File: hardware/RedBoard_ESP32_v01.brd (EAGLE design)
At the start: 68.6 x 58.4 mm, 211 parts, among them J1 5.5x2.1mm Barrel, J13 QWIIC_RIGHT_ANGLE, J15 MICRO-SD-PUSH-PUSH-EXT-PIN, J2 USB C, J3 USB_SOLDER_PADS, J5 M10NO_SILK, Q1 MBT3904DW1T1, Q11 20V/4.2A/52mΩ/1.4W, Q13 20V/4.2A/52mΩ/1.4W, Q3 20V/4.2A/52mΩ/1.4W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

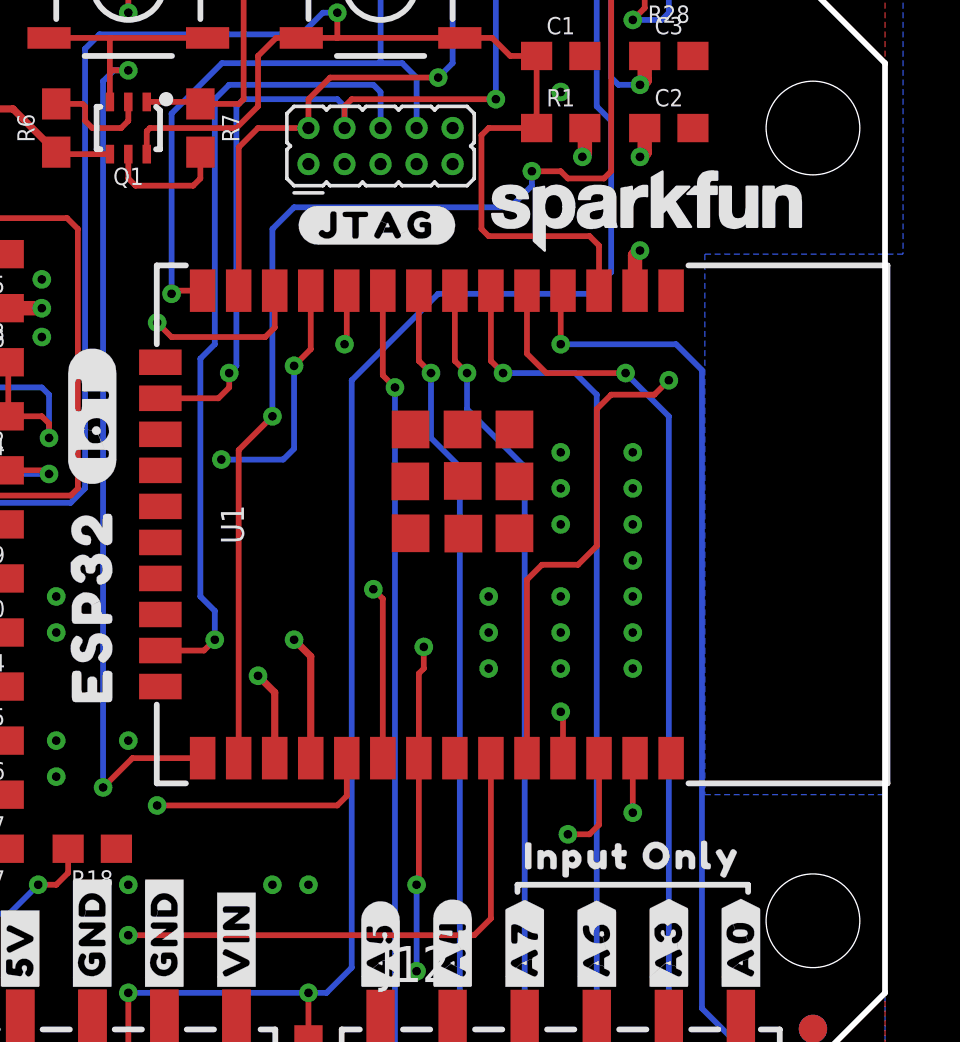
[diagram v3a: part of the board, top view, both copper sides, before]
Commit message: Updated silkscreen.
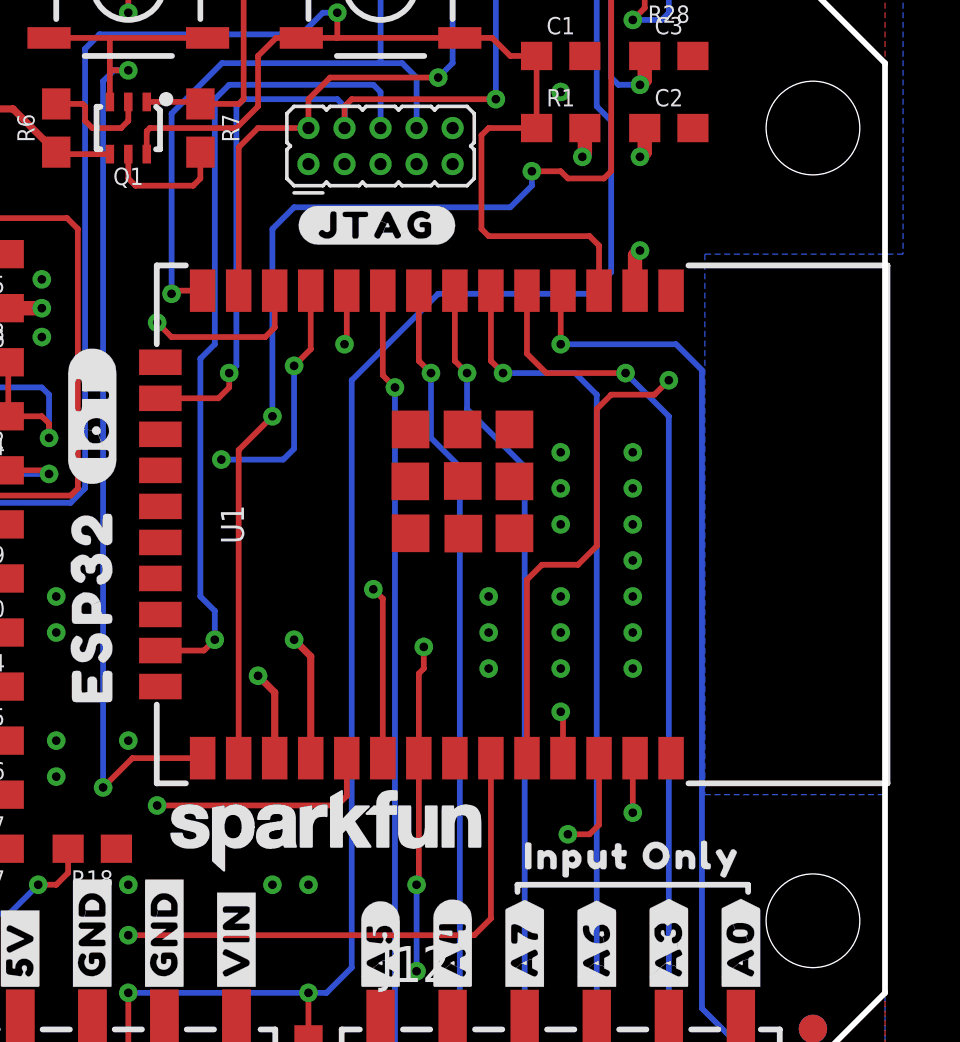
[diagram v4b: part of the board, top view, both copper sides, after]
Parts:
- moved LOGO1 24.6 mm to (48.9, 13.3)
- moved U$47 11.3 mm to (26.2, 32.6)
- moved U$93 1.91 mm to (40.0, 21.5)
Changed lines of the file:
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@@
 <drawing>
 <settings>
-<setting alwaysvectorfont="no"/>
+<setting alwaysvectorfont="yes"/>
 <setting keepoldvectorfont="yes"/>
 <setting verticaltext="up"/>
@@
 <grid distance="0.05" unitdist="inch" unit="inch" style="lines" multiple="1" display="yes" altdistance="0.005" altunitdist="inch" altunit="inch"/>
 <layers>
-<layer number="1" name="Top" color="4" fill="1" visible="yes" active="yes"/>
-<layer number="2" name="Route2" color="24" fill="1" visible="yes" active="yes"/>
-<layer number="15" name="Route15" color="23" fill="1" visible="yes" active="yes"/>
-<layer number="16" name="Bottom" color="1" fill="1" visible="yes" active="yes"/>
-<layer number="17" name="Pads" color="2" fill="1" visible="yes" active="yes"/>
-<layer number="18" name="Vias" color="2" fill="1" visible="yes" active="yes"/>
-<layer number="19" name="Unrouted" color="6" fill="1" visible="yes" active="yes"/>
+<layer number="1" name="Top" color="4" fill="1" visible="no" active="yes"/>
+<layer number="2" name="Route2" color="24" fill="1" visible="no" active="yes"/>
+<layer number="15" name="Route15" color="23" fill="1" visible="no" active="yes"/>
+<layer number="16" name="Bottom" color="1" fill="1" visible="no" active="yes"/>
+<layer number="17" name="Pads" color="2" fill="1" visible="no" active="yes"/>
+<layer number="18" name="Vias" color="2" fill="1" visible="no" active="yes"/>
+<layer number="19" name="Unrouted" color="6" fill="1" visible="no" active="yes"/>
 <layer number="20" name="Dimension" color="24" fill="1" visible="yes" active="yes"/>
 <layer number="21" name="tPlace" color="16" fill="1" visible="yes" active="yes"/>
@@
 <layer number="23" name="tOrigins" color="15" fill="1" visible="yes" active="yes"/>
 <layer number="24" name="bOrigins" color="15" fill="1" visible="yes" active="yes"/>
-<layer number="25" name="tNames" color="7" fill="1" visible="yes" active="yes"/>
-<layer number="26" name="bNames" color="7" fill="1" visible="yes" active="yes"/>
-<layer number="27" name="tValues" color="7" fill="1" visible="yes" active="yes"/>
-<layer number="28" name="bValues" color="7" fill="1" visible="yes" active="yes"/>
-<layer number="29" name="tStop" color="7" fill="3" visible="yes" active="yes"/>
-<layer number="30" name="bStop" color="7" fill="6" visible="yes" active="yes"/>
-<layer number="31" name="tCream" color="7" fill="4" visible="yes" active="yes"/>
-<layer number="32" name="bCream" color="7" fill="5" visible="yes" active="yes"/>
-<layer number="33" name="tFinish" color="6" fill="3" visible="yes" active="yes"/>
-<layer number="34" name="bFinish" color="6" fill="6" visible="yes" active="yes"/>
-<layer number="35" name="tGlue" color="7" fill="4" visible="yes" active="yes"/>
-<layer number="36" name="bGlue" color="7" fill="5" visible="yes" active="yes"/>
-<layer number="37" name="tTest" color="7" fill="1" visible="yes" active="yes"/>
-<layer number="38" name="bTest" color="7" fill="1" visible="yes" active="yes"/>
-<layer number="39" name="tKeepout" color="4" fill="11" visible="yes" active="yes"/>
-<layer number="40" name="bKeepout" color="1" fill="11" visible="yes" active="yes"/>
-<layer number="41" name="tRestrict" color="4" fill="10" visible="yes" active="yes"/>
-<layer number="42" name="bRestrict" color="1" fill="10" visible="yes" active="yes"/>
-<layer number="43" name="vRestrict" color="2" fill="10" visible="yes" active="yes"/>
-<layer number="44" name="Drills" color="7" fill="1" visible="yes" active="yes"/>
-<layer number="45" name="Holes" color="7" fill="1" visible="yes" active="yes"/>
-<layer number="46" name="Milling" color="3" fill="1" visible="yes" active="yes"/>
-<layer number="47" name="Measures" color="7" fill="1" visible="yes" active="yes"/>
+<layer number="25" name="tNames" color="7" fill="1" visible="no" active="yes"/>
+<layer number="26" name="bNames" color="7" fill="1" visible="no" active="yes"/>
+<layer number="27" name="tValues" color="7" fill="1" visible="no" active="yes"/>
+<layer number="28" name="bValues" color="7" fill="1" visible="no" active="yes"/>
+<layer number="29" name="tStop" color="7" fill="3" visible="no" active="yes"/>
+<layer number="30" name="bStop" color="7" fill="6" visible="no" active="yes"/>
+<layer number="31" name="tCream" color="7" fill="4" visible="no" active="yes"/>
+<layer number="32" name="bCream" color="7" fill="5" visible="no" active="yes"/>
+<layer number="33" name="tFinish" color="6" fill="3" visible="no" active="yes"/>
+<layer number="34" name="bFinish" color="6" fill="6" visible="no" active="yes"/>
+<layer number="35" name="tGlue" color="7" fill="4" visible="no" active="yes"/>
+<layer number="36" name="bGlue" color="7" fill="5" visible="no" active="yes"/>
+<layer number="37" name="tTest" color="7" fill="1" visible="no" active="yes"/>
+<layer number="38" name="bTest" color="7" fill="1" visible="no" active="yes"/>
+<layer number="39" name="tKeepout" color="4" fill="11" visible="no" active="yes"/>
+<layer number="40" name="bKeepout" color="1" fill="11" visible="no" active="yes"/>
+<layer number="41" name="tRestrict" color="4" fill="10" visible="no" active="yes"/>
+<layer number="42" name="bRestrict" color="1" fill="10" visible="no" active="yes"/>
+<layer number="43" name="vRestrict" color="2" fill="10" visible="no" active="yes"/>
+<layer number="44" name="Drills" color="7" fill="1" visible="no" active="yes"/>
+<layer number="45" name="Holes" color="7" fill="1" visible="no" active="yes"/>
+<layer number="46" name="Milling" color="3" fill="1" visible="no" active="yes"/>
+<layer number="47" name="Measures" color="7" fill="1" visible="no" active="yes"/>
 <layer number="48" name="Document" color="7" fill="1" visible="yes" active="yes"/>
-<layer number="49" name="Reference" color="7" fill="1" visible="yes" active="yes"/>
-<layer number="50" name="dxf" color="7" fill="1" visible="yes" active="yes"/>
+<layer number="49" name="Reference" color="7" fill="1" visible="no" active="yes"/>
+<layer number="50" name="dxf" color="7" fill="1" visible="no" active="yes"/>
 <layer number="51" name="tDocu" color="6" fill="1" visible="yes" active="yes"/>
 <layer number="52" name="bDocu" color="7" fill="1" visible="yes" active="yes"/>
@@
 <attribute name="VALUE" x="31.75" y="38.4175" size="0.6096" layer="27" font="vector" ratio="20" rot="R180" align="top-center"/>
 </element>
-<element name="LOGO1" library="SparkFun-Aesthetics" package="SFE_LOGO_NAME_.1" value="SFE_LOGO_NAME.1_INCH" x="60.198" y="35.179" smashed="yes"/>
+<element name="LOGO1" library="SparkFun-Aesthetics" package="SFE_LOGO_NAME_.1" value="SFE_LOGO_NAME.1_INCH" x="48.895" y="13.335" smashed="yes"/>
 <element name="LOGO2" library="SparkFun-Aesthetics" package="QWIIC_5MM" value="QWIIC_LOGO_5MM" x="10.16" y="51.562" smashed="yes"/>
 <element name="LOGO3" library="SparkFun-Aesthetics" package="OSHW-LOGO-MINI" value="OSHW-LOGOMINI" x="2.286" y="2.032" smashed="yes" rot="MR0"/>
@@
 <element name="U$98" library="SparkFun-Aesthetics" package="REDBOARD_LOGO" value="" x="45.72" y="22.86" smashed="yes" rot="MR0"/>
 <element name="U$100" library="output-ESP32" package="#IOT#132321869" value="" x="40.64" y="27.94" smashed="yes" rot="R90"/>
-<element name="U$93" library="output-ESP32" package="ESP32321856" value="" x="38.1" y="21.463" smashed="yes" rot="MR0"/>
-<element name="U$47" library="output-ESP32" package="#IOT#132321874" value="" x="27.94" y="21.463" smashed="yes" rot="MR0"/>
+<element name="U$93" library="output-ESP32" package="ESP32321856" value="" x="40.005" y="21.463" smashed="yes" rot="MR0"/>
+<element name="U$47" library="output-ESP32" package="#IOT#132321874" value="" x="26.162" y="32.639" smashed="yes" rot="MR0"/>
 <element name="U$94" library="output-ESP32" package="MADE_IN32321857" value="" x="34.29" y="16.51" smashed="yes" rot="MR0"/>
 <element name="U$99" library="output-ESP32" package="THE_USA32321858" value="" x="34.29" y="13.97" smashed="yes" rot="MR0"/>
